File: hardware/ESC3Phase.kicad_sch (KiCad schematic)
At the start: 0 parts

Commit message: Add hierarchical sheet skeleton and library wiring
- 6 sub-sheets (Power Supply, MCU Core, Gate Drive, Power Stage,
  Current Sensing, Communication) wired into the root sheet
- Title blocks + text variables (PROJECT_NAME/DESIGNER/PROJECTNUMBER)
  and METU PowerLab drawing sheet template on every sheet
- GND (blue)/Power (red) net classes with name-pattern auto-assignment
- Project-local sym-lib-table/fp-lib-table covering every
  PowerLabKiCadLibraries library plus the new ESP32 library, so the
  schematic tooling can actually place these parts (worked around a
  tool quirk: it only resolves project-scope tables written via the
  register_* tools, not global-scope or hand-edited project tables)
- ESP32-WROOM-32E (U1) placed on the MCU Core sheet
- ARCHITECTURE.md documenting every component selection and rationale,
  sourced from the actual installed PowerLabKiCadLibraries contents

Co-Authored-By: Claude Sonnet 5 <noreply@anthropic.com>
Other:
- added sheet Communication (Communication.kicad_sch)
- added sheet Current Sensing (CurrentSensing.kicad_sch)
- added sheet Gate Drive (GateDrive.kicad_sch)
- added sheet MCU Core (MCUCore.kicad_sch)
- added sheet Power Stage (PowerStage.kicad_sch)
- added sheet Power Supply (PowerSupply.kicad_sch)
- note added: "ESC3Phase — 3-Phase BLDC/PMSM Electronic Speed Controller MCU: ESP32-WROOM-32E (SMD, direct-soldered) | Vin: 12-36V DC | Target: ~5-10A continuous/phase Control: UART (also flashing interface) + CAN (TWAI) | Current sensing: DRV8323 per-phase + DC-bus INA240 2-layer PCB, PCBWay standard-price spec"
- company: (none) -> METU PowerLab
- title: (none) -> ${PROJECT_NAME}
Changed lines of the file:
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@@
 (kicad_sch (version 20260101) (generator "eeschema") (generator_version "10.0")
   (paper "A4")
+  (title_block
+    (title "${PROJECT_NAME}")
+    (date "2026-09-27")
+    (rev "A")
+    (company "METU PowerLab")
+    (comment 1 "Designer: ${DESIGNER}")
+    (comment 2 "Project No: ${PROJECTNUMBER}")
+  )
+  (sheet (at 20.0 30.0) (size 60.0 35.0) (fields_autoplaced yes)
+    (stroke (width 0.0006) (type default))
+    (fill (color 0 0 0 0.0000))
+    (property "Sheet name" "Power Supply" (at 22.54 28.73 0)
+      (effects (font (size 1.27 1.27)) (justify left bottom))
+    )
+    (property "Sheet file" "PowerSupply.kicad_sch" (at 22.54 66.27 0)
+      (effects (font (size 1.27 1.27)) (justify left bottom))
+    )
+  )
+  (sheet (at 100.0 30.0) (size 60.0 35.0) (fields_autoplaced yes)
+    (stroke (width 0.0006) (type default))
+    (fill (color 0 0 0 0.0000))
+    (property "Sheet name" "MCU Core" (at 102.54 28.73 0)
+      (effects (font (size 1.27 1.27)) (justify left bottom))
+    )
+    (property "Sheet file" "MCUCore.kicad_sch" (at 102.54 66.27 0)
+      (effects (font (size 1.27 1.27)) (justify left bottom))
+    )
+  )
+  (sheet (at 180.0 30.0) (size 60.0 35.0) (fields_autoplaced yes)
+    (stroke (width 0.0006) (type default))
+    (fill (color 0 0 0 0.0000))
+    (property "Sheet name" "Gate Drive" (at 182.54 28.73 0)
+      (effects (font (size 1.27 1.27)) (justify left bottom))
+    )
+    (property "Sheet file" "GateDrive.kicad_sch" (at 182.54 66.27 0)
+      (effects (font (size 1.27 1.27)) (justify left bottom))
+    )
+  )
+  (sheet (at 20.0 90.0) (size 60.0 35.0) (fields_autoplaced yes)
+    (stroke (width 0.0006) (type default))
+    (fill (color 0 0 0 0.0000))
+    (property "Sheet name" "Power Stage" (at 22.54 88.73 0)
+      (effects (font (size 1.27 1.27)) (justify left bottom))
+    )
+    (property "Sheet file" "PowerStage.kicad_sch" (at 22.54 126.27 0)
+      (effects (font (size 1.27 1.27)) (justify left bottom))
+    )
+  )
+  (sheet (at 100.0 90.0) (size 60.0 35.0) (fields_autoplaced yes)
+    (stroke (width 0.0006) (type default))
+    (fill (color 0 0 0 0.0000))
+    (property "Sheet name" "Current Sensing" (at 102.54 88.73 0)
+      (effects (font (size 1.27 1.27)) (justify left bottom))
+    )
+    (property "Sheet file" "CurrentSensing.kicad_sch" (at 102.54 126.27 0)
+      (effects (font (size 1.27 1.27)) (justify left bottom))
+    )
+  )
+  (sheet (at 180.0 90.0) (size 60.0 35.0) (fields_autoplaced yes)
+    (stroke (width 0.0006) (type default))
+    (fill (color 0 0 0 0.0000))
+    (property "Sheet name" "Communication" (at 182.54 88.73 0)
+      (effects (font (size 1.27 1.27)) (justify left bottom))
+    )
+    (property "Sheet file" "Communication.kicad_sch" (at 182.54 126.27 0)
+      (effects (font (size 1.27 1.27)) (justify left bottom))
+    )
+  )
+	(text "ESC3Phase — 3-Phase BLDC/PMSM Electronic Speed Controller\nMCU: ESP32-WROOM-32E (SMD, direct-soldered)  |  Vin: 12-36V DC  |  Target: ~5-10A continuous/phase\nControl: UART (also flashing interface) + CAN (TWAI)  |  Current sensing: DRV8323 per-phase + DC-bus INA240\n2-layer PCB, PCBWay standard-price spec"
+		(exclude_from_sim no)
+		(at 20 12 0)
+		(effects
+			(font
+				(size 1.5 1.5)
+			)
+			(justify left bottom)
+		)
+	)
   (sheet_instances
     (path "/" (page "1"))
+      (path "/cbc0567c-ebb2-4f69-aedb-b6520912ec49/0e36a24c-e528-4ce2-929f-e01aaf3d5fc1" (page "2"))
+      (path "/cbc0567c-ebb2-4f69-aedb-b6520912ec49/a4f87701-db4b-4c47-a6ec-e1866c2da18c" (page "3"))
+      (path "/cbc0567c-ebb2-4f69-aedb-b6520912ec49/98c91055-e4de-4d26-8de4-bfe1e1746b6b" (page "4"))
+      (path "/cbc0567c-ebb2-4f69-aedb-b6520912ec49/7ad74ea6-21b1-4cd1-950e-4b757b527b6e" (page "5"))
+      (path "/cbc0567c-ebb2-4f69-aedb-b6520912ec49/ff2f6218-521d-4507-8ae5-5c0517620d4d" (page "6"))
+      (path "/cbc0567c-ebb2-4f69-aedb-b6520912ec49/28d327bd-5418-4f26-bfa2-4ace7d3b7dc9" (page "7"))
   )
 )

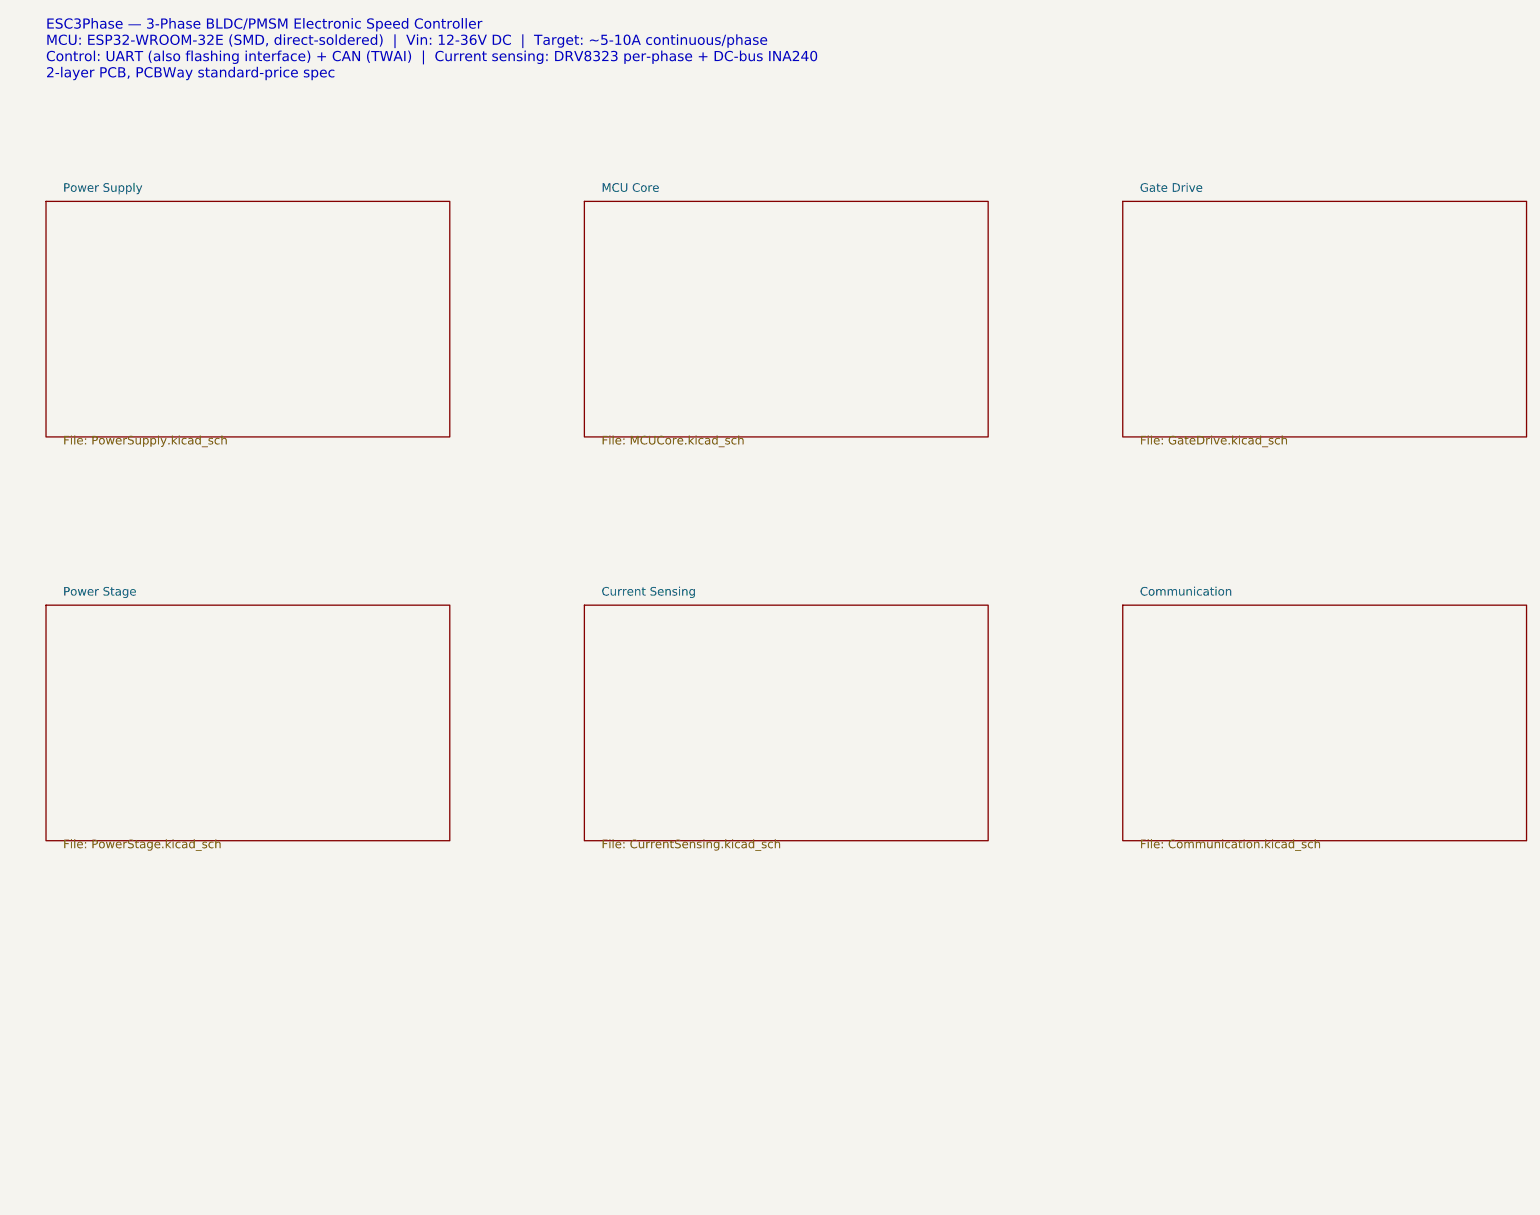
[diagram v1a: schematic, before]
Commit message: Schematic Rev B: full rebuild per METU PowerLab rules
Rev A was withdrawn: labels stuck on pins created real net shorts
(+5V_LOGIC with the 36 V bus, INHA and EFUSE_IMON with GND) and several
circuits contradicted their datasheets.

Rev B: real wires and power symbols on the 2.54 mm grid, hierarchical sheets
(half bridge reused 3x), library values, LAYOUT notes, root page with specs
and block diagram. Circuit fixes: DRV8323 VREF driven, unused buck tied to
GND, INA240A1, LM74700-Q1 reverse polarity, SMBJ36CA, eFuse per datasheet,
direct 3.3 V buck, 4.7 uH/8.1 A inductor, 2512 shunts with net-tie Kelvin,
24 V CAN ESD. kicad-cli ERC: 0 errors; netlist matches intent on all nets.
Old board and project-local library tables removed (board is rebuilt next).

Co-Authored-By: Claude Opus 5.5 <noreply@anthropic.com>
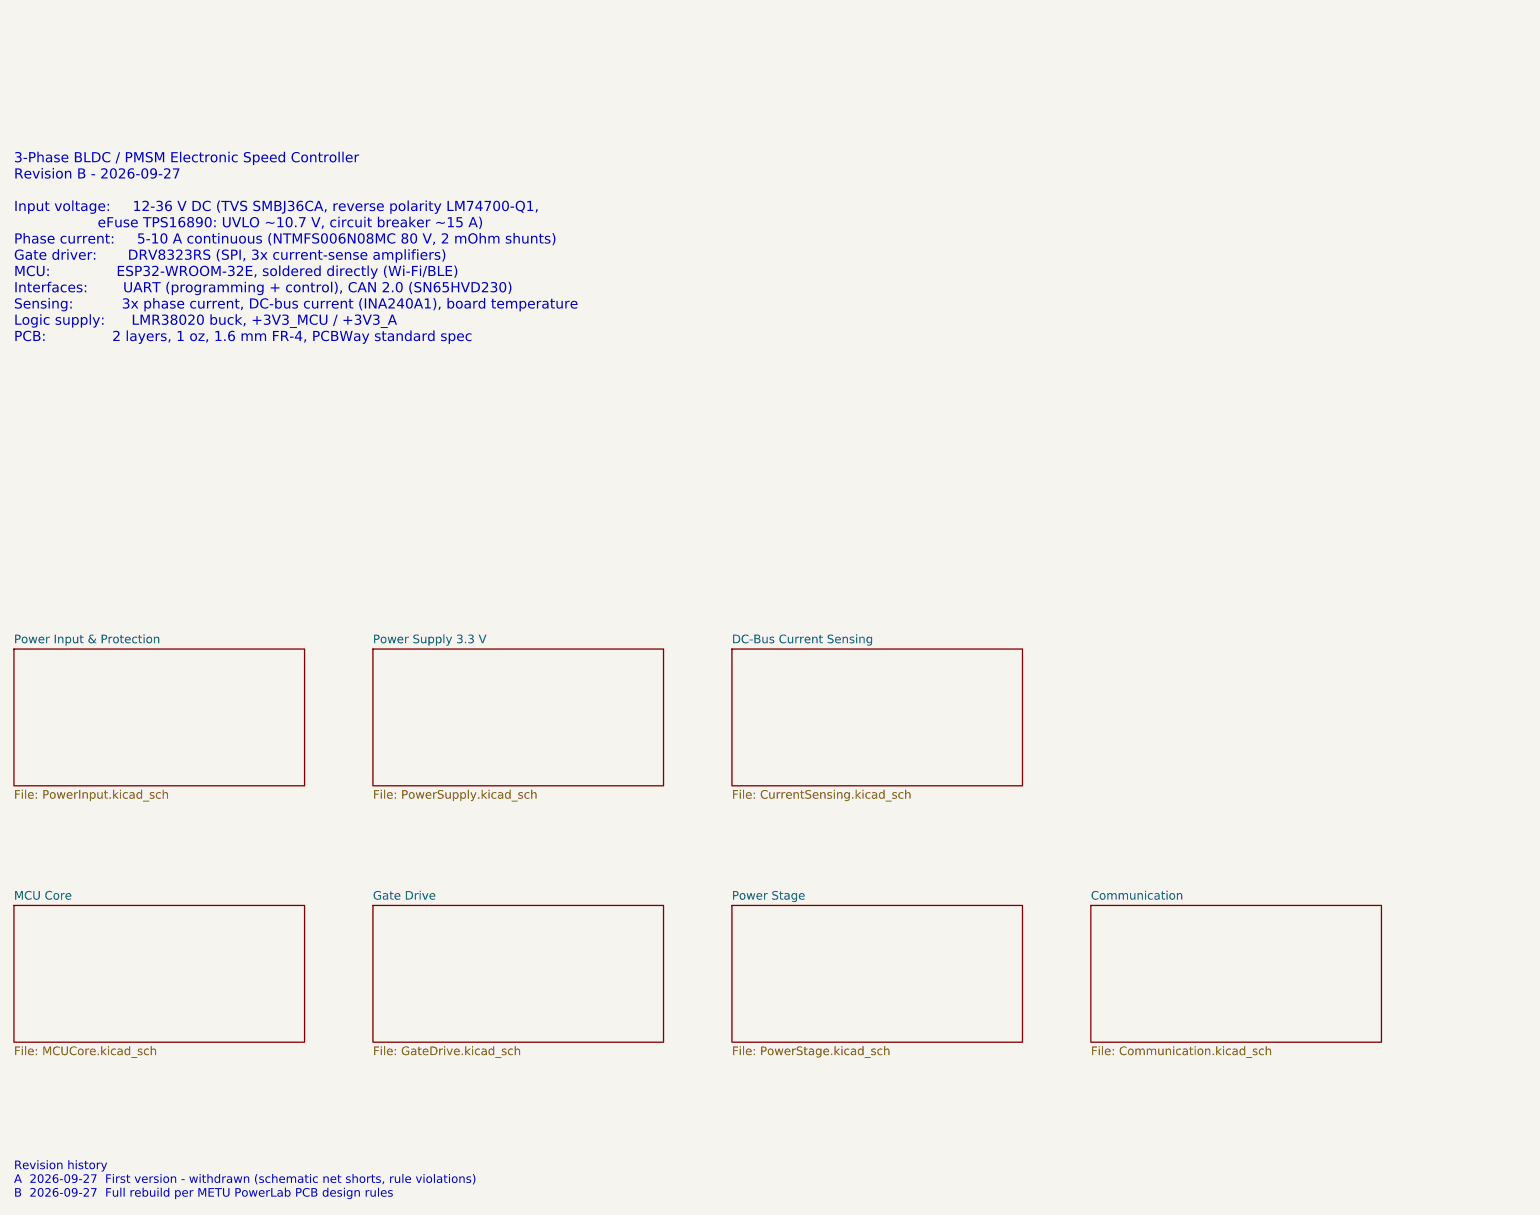
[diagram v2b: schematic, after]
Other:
- removed sheet Current Sensing
- removed sheet Power Supply
- added sheet DC-Bus Current Sensing (CurrentSensing.kicad_sch)
- added sheet Power Input & Protection (PowerInput.kicad_sch)
- added sheet Power Supply 3.3 V (PowerSupply.kicad_sch)
- note added: "3-Phase BLDC / PMSM Electronic Speed Controller Revision B - 2026-09-27 Input voltage: 12-36 V DC (TVS SMBJ36CA, reverse polarity LM74700-Q1, eFuse TPS16890: UVLO ~10.7 V, circuit breaker ~15 A) Phase current: 5-10 A continuous (NTMFS006N08MC 80 V, 2 mOhm shunts) Gate driver: DRV8323RS (SPI, 3x current-sense amplifiers) MCU: ESP32-WROOM-32E, soldered directly (Wi-Fi/BLE) Interfaces: UART (program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"
- note added: "Revision history A 2026-09-27 First version - withdrawn (schematic net shorts, rule violations) B 2026-09-27 Full rebuild per METU PowerLab PCB design rules"
- note removed: "ESC3Phase — 3-Phase BLDC/PMSM Electronic Speed Controller MCU: ESP32-WROOM-32E (SMD, direct-soldered) | Vin: 12-36V DC | Target: ~5-10A continuous/phase Control: UART (also flashing interface) + CAN (TWAI) | Current sensing: DRV8323 per-phase + DC-bus INA240 2-layer PCB, PCBWay standard-price spec"
- title: ${PROJECT_NAME} -> 3-Phase BLDC ESC - Overview
